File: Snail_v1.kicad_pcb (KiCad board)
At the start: 4 copper layers, 92.6 x 22.8 mm, 87 parts, among them J1 PWM_Connector, J2 Conn_ARM_SWD_TagConnect_TC203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, J3 USB_C_Receptacle_USB2.0_16P, J4 OUT+, J5 OUT-, J6 Conn_01x01, J7 Conn_01x01, U1 STM32G431K6Tx, U2 TLV61070ADBV, U3 BQ24074RGT, U4 82400102, U5 TPS63031DSK, U6 FUSB303BTMX, U7 BY25Q32ES, U8 PAM8302AAS

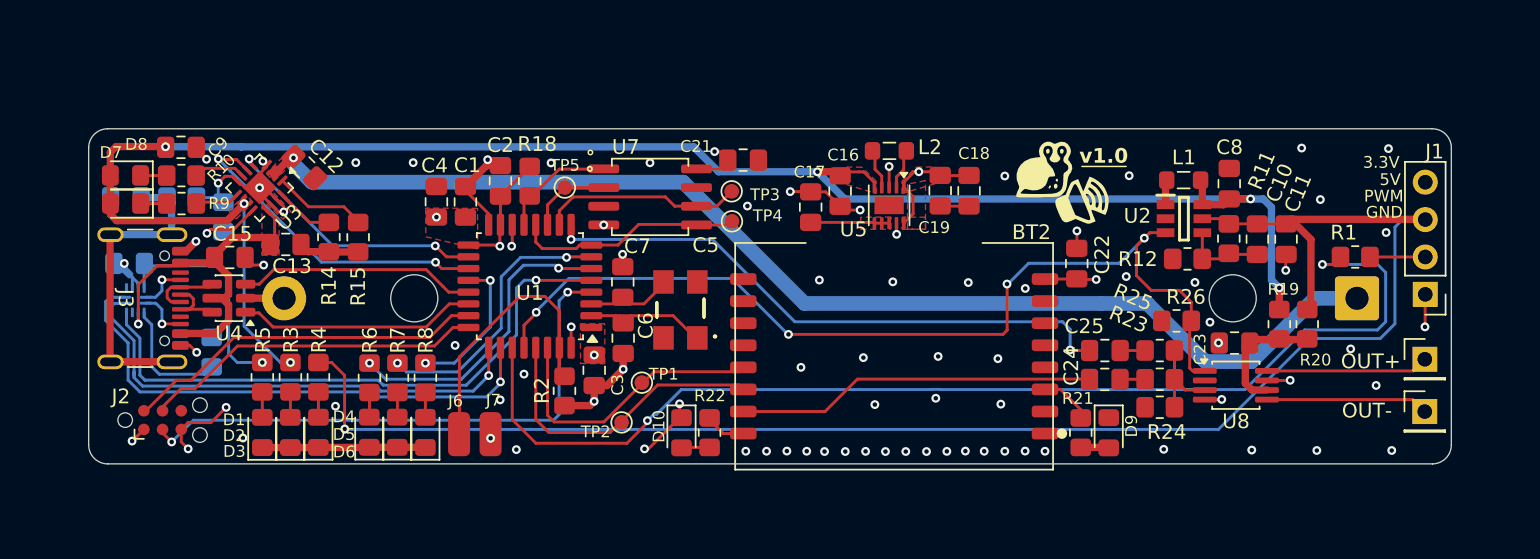
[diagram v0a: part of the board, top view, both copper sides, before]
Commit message: Changed layout + added dimensions
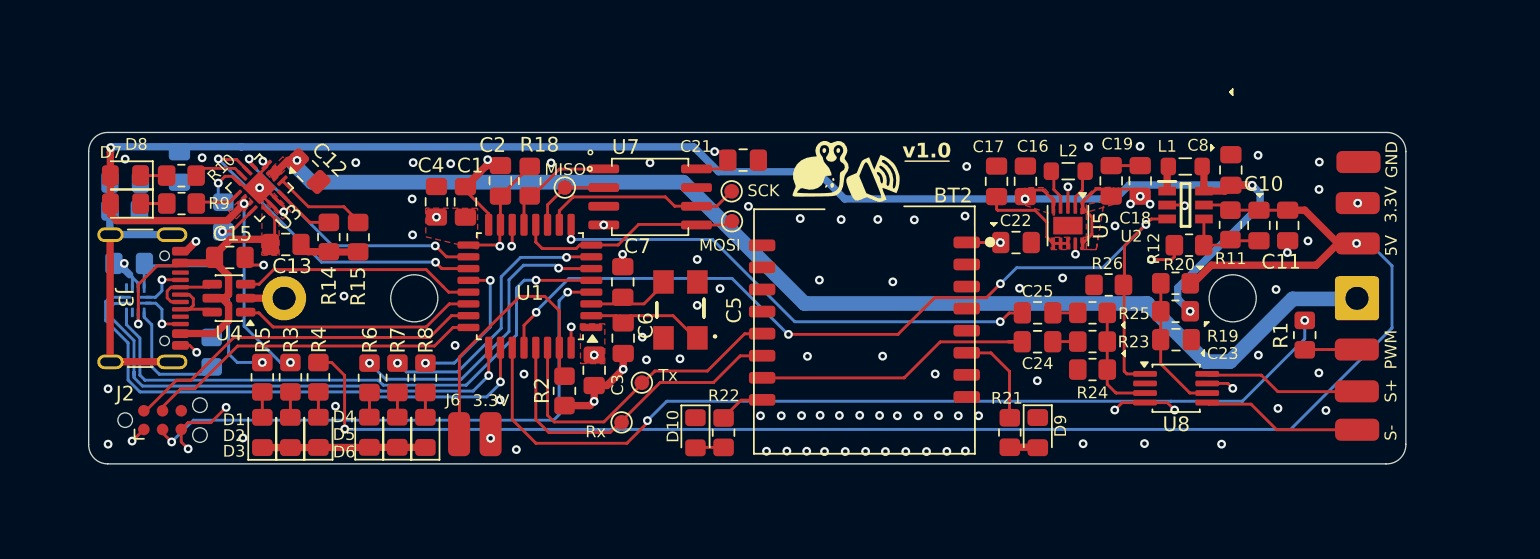
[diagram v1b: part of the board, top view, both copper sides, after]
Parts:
- added J10: Conn_01x01, Connector_Wire:SolderWirePad_1x01_SMD_1.5x3mm, F.Cu at (133.8, 108.8)
- added J8: Conn_01x01, Connector_Wire:SolderWirePad_1x01_SMD_1.5x3mm, F.Cu at (133.7, 114.3)
- added J9: Conn_01x01, Connector_Wire:SolderWirePad_1x01_SMD_1.5x3mm, F.Cu at (133.6, 121.5)
- C9: moved to B.Cu
- J1: value PWM_Connector -> Conn_01x01; footprint Connector_PinHeader_2.54mm:PinHeader_1x04_P2.54mm_Vertical -> Connector_Wire:SolderWirePad_1x01_SMD_1.5x3mm
- J4, J5: footprint Connector_PinHeader_2.54mm:PinHeader_1x01_P2.54mm_Vertical -> Connector_Wire:SolderWirePad_1x01_SMD_1.5x3mm
- moved G*** 15.2 mm to (97.1, 109.2)
- moved G*** 14.3 mm to (100.8, 110.0)
- moved C17 12.8 mm to (109.2, 110.1)
- moved C16 12.6 mm to (111.1, 110.1), turned to 90 degrees
- moved L2 12.2 mm to (114.0, 109.4)
- moved U5 12.2 mm to (114.0, 113.1)
- moved C18 11.6 mm to (118.9, 110.0), turned to 90 degrees
- moved C19 11.6 mm to (117.0, 110.0), turned to 90 degrees
- moved R20 9.37 mm to (121.3, 117.0), turned to 180 degrees
- moved J1 7.71 mm to (133.7, 111.5), turned to -90 degrees
- moved R19 7.10 mm to (121.3, 118.9), turned to 180 degrees
- moved R1 6.32 mm to (130.1, 120.5), turned to -90 degrees
- moved BT2 5.87 mm to (96.9, 119.5)
- moved C24 5.24 mm to (111.9, 121.0)
- moved C25 5.24 mm to (112.0, 119.0)
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- renumbered J7 to 3.3V, TP5 to MISO, TP4 to MOSI, TP2 to Rx, TP3 to SCK, TP1 to Tx
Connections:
- J1 pad 1: GND -> +3V3
- R1 pad 2: Net-(J1-Pin_2) -> Net-(J9-Pin_1)
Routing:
- net PWM: track 77.8 -> 63.7 mm
- net GND: track 85.0 -> 76.5 mm, vias 83 -> 102
- net MCU_AUDIO: track 40.2 -> 34.6 mm
- net Net-(BT2-AUDIO): track 24.4 -> 19.8 mm
- net Net-(J1-Pin_2): track 4.41 -> 0.00 mm
- net Net-(J9-Pin_1): track 0.00 -> 3.55 mm
- net Net-(BT2-STAT): track 3.56 -> 6.55 mm
- net UART1_Tx: track 19.6 -> 22.0 mm
- net Net-(U3-ILIM): track 5.02 -> 2.69 mm
- net 5V_EN: track 65.6 -> 63.6 mm
- net UART1_Rx: track 20.8 -> 22.9 mm
- net Net-(U5-EN): track 5.35 -> 7.33 mm
- net +OUT: track 124.4 -> 126.4 mm
- net Net-(U8-IN+): track 6.23 -> 7.68 mm
- net Net-(U8-VDD): track 8.75 -> 9.89 mm
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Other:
- board size 92.6 x 22.8 mm -> 89.5 x 22.5 mm
- board text added: "S+"
- board text added: "S-"
- board text removed: "OUT+"
- board text removed: "OUT-"

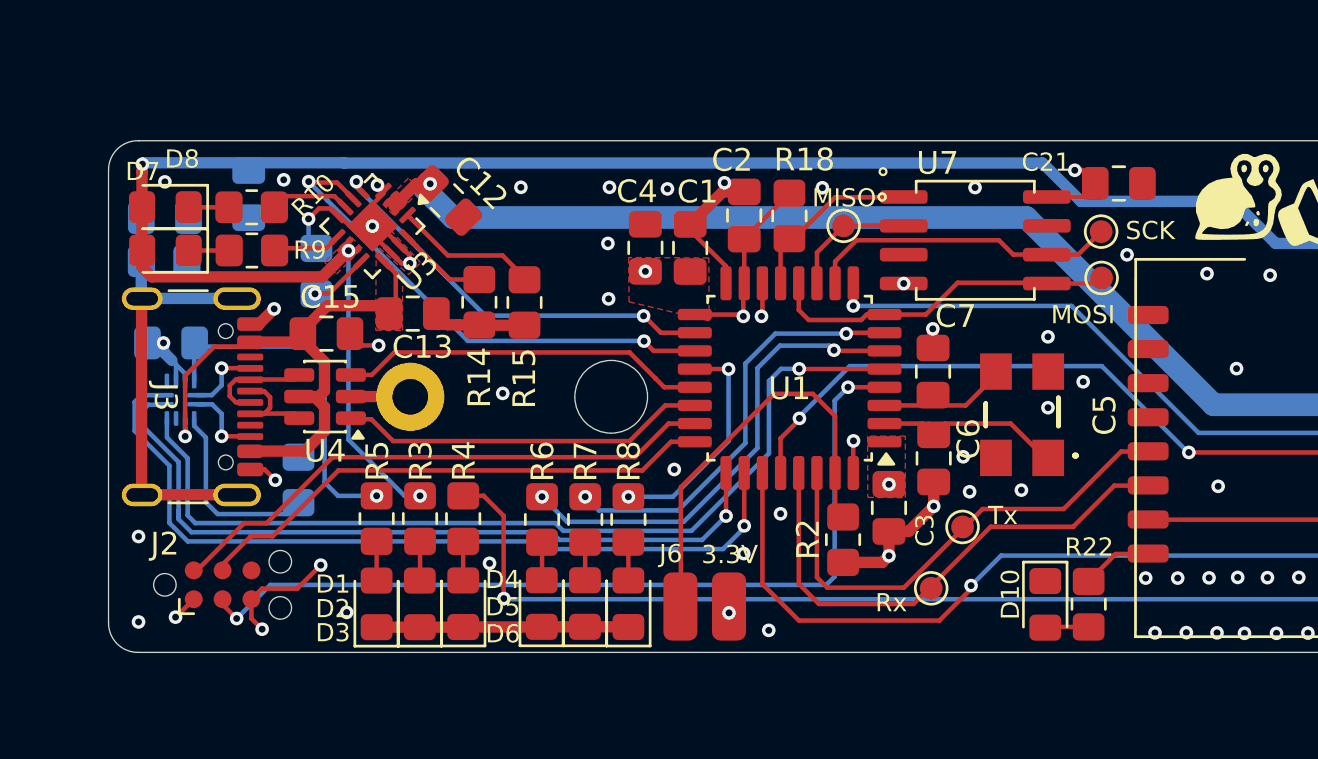
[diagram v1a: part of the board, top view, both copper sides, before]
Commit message: Added +BAT and GND Pad to design
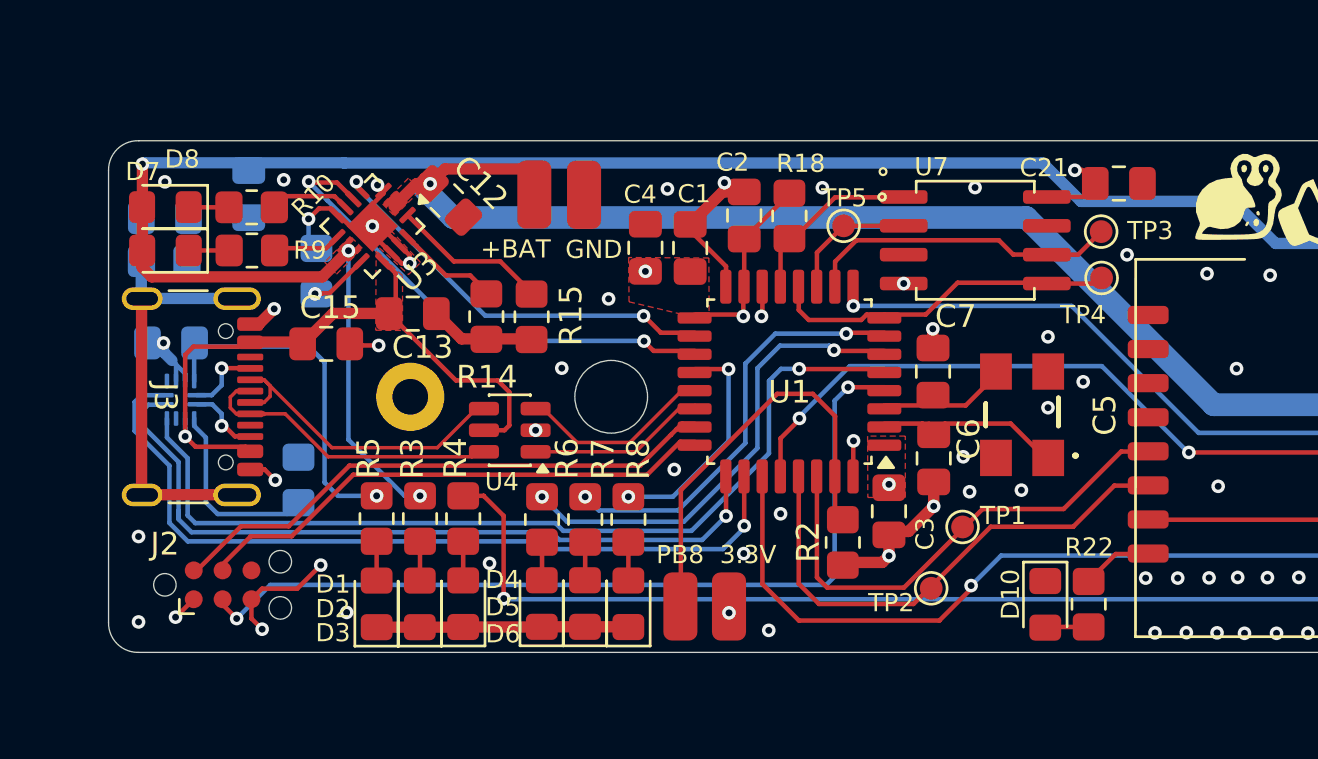
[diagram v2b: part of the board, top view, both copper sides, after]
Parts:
- added +BAT: Conn_01x01, Connector_Wire:SolderWirePad_1x01_SMD_1.5x3mm, F.Cu at (66.2, 109.1)
- added GND: Conn_01x01, Connector_Wire:SolderWirePad_1x01_SMD_1.5x3mm, F.Cu at (68.4, 109.1)
- moved U4 8.26 mm to (65.1, 119.5)
- moved R14 0.70 mm to (64.1, 114.5)
- moved R15 0.70 mm to (66.1, 114.5)
- moved C15 0.45 mm to (57.0, 115.7)
- moved U1 0.15 mm to (77.4, 117.3)
- moved C3 0.15 mm to (81.8, 123.0)
- moved R2 0.12 mm to (79.8, 124.4)
- renumbered J6 to PB8, Tx to TP1, Rx to TP2, SCK to TP3, MOSI to TP4, MISO to TP5
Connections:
- net Net-(BT1-+) renamed +BAT
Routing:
- net Net-(J3-D--PadA7): track 4.70 -> 14.1 mm
- net Net-(J3-D+-PadA6): track 5.92 -> 14.6 mm
- net USB+: track 16.2 -> 7.94 mm
- net USB-: track 16.2 -> 8.63 mm
- net +BAT: track 82.1 -> 87.7 mm
- net /USB_and_Power/VBUS: track 26.3 -> 29.4 mm
- net GND: track 76.5 -> 74.5 mm, vias 102 -> 100
- net Net-(U3-ISET): track 3.93 -> 4.80 mm
- net Net-(U3-TS): track 6.40 -> 6.99 mm
